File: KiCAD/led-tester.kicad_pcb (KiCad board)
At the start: 2 copper layers, 21 parts, among them IC1 ATMEGA328P-A, P1 CONN_02X07, P2 CONN_01X06, P3 CONN_02X03, U1 MCP1702-5002E

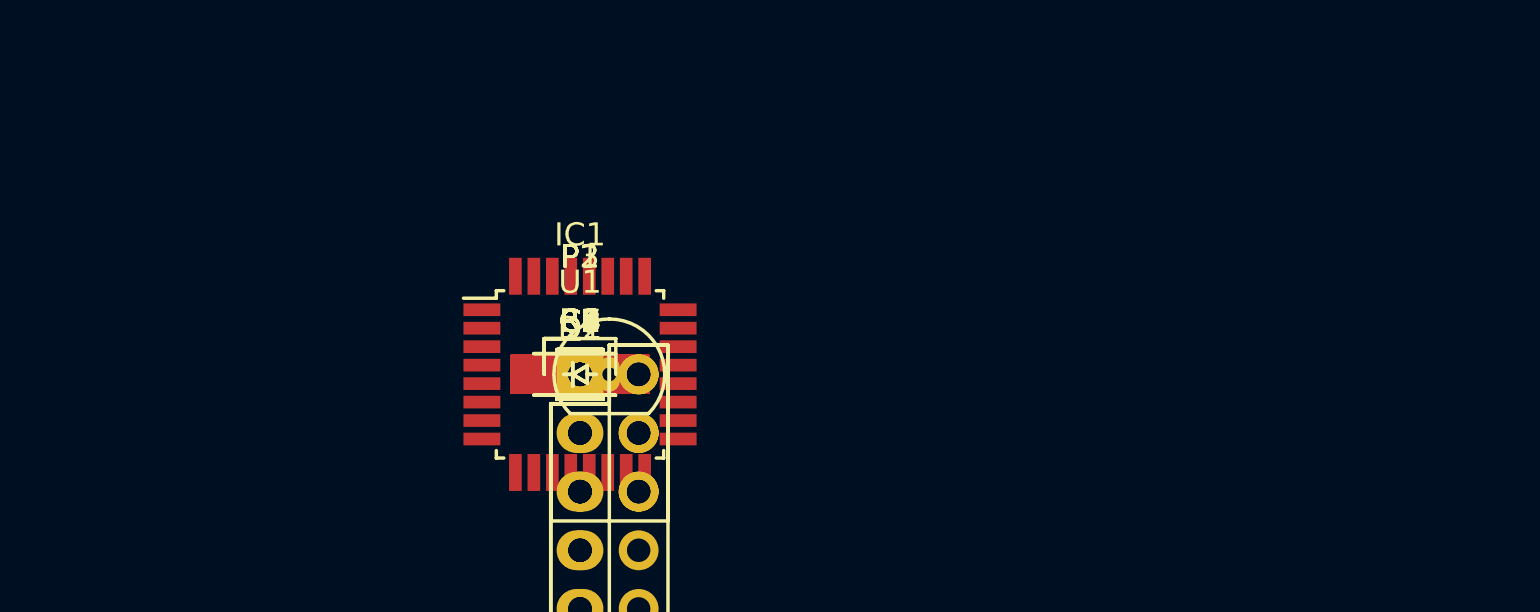
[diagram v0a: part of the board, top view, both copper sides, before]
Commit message: added footprint for led test pads and added pin numbers
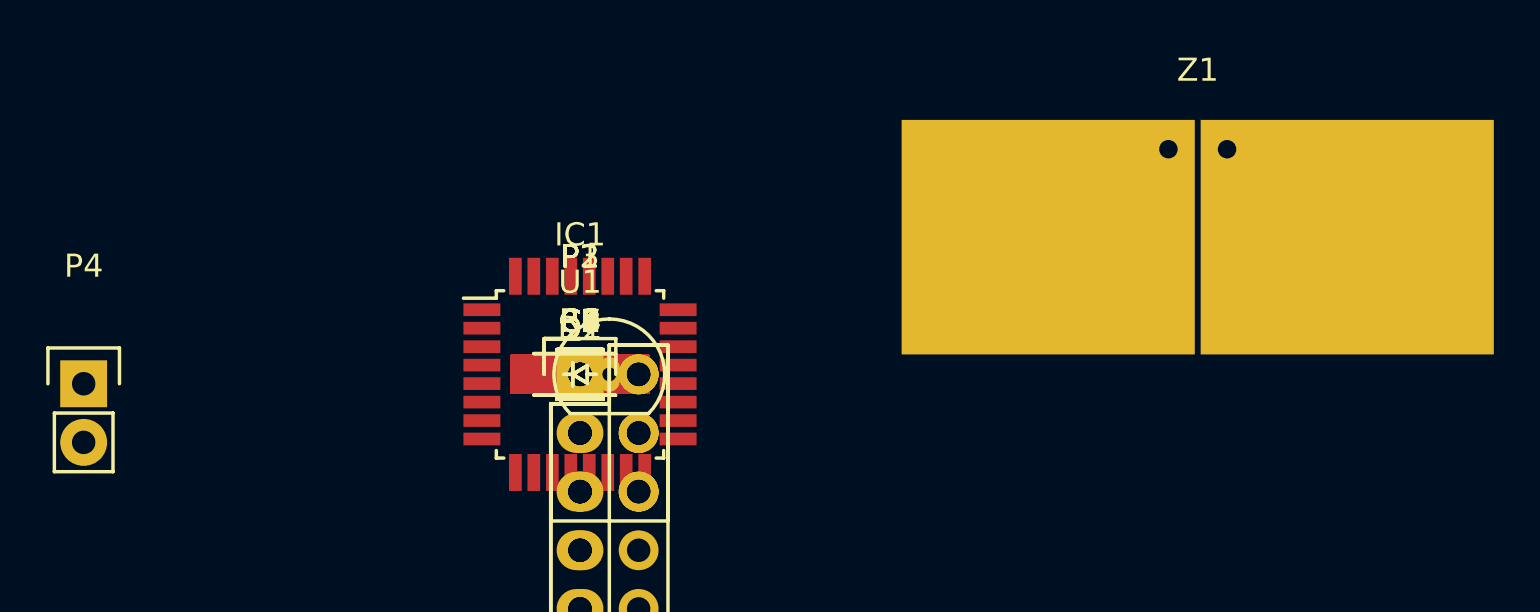
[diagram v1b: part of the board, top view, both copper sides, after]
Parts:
- added P4: CONN_01X02, Pin_Headers:Pin_Header_Straight_1x02, F.Cu at (127.0, 105.4)
- added Z1: testPad, led-tester:LED-LargePads, F.Cu at (175.3, 95.2)
- C1: value 1 uF -> 0.1 uF
- C2: value 0.1 uF -> 1 uF
- C3: value 0.1 uF -> 0.1uF
- C4: value 10 nF -> 0.1uF
- IC1: value ATMEGA328P-A -> ATTINY1634R-SU
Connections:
- C2 pad 1: Net-(C2-Pad1) -> +5V
- C3 pad 1: +5V -> +9V
- C4 pad 1: Net-(C4-Pad1) -> LEDlow
- C5 pad 1: +9V -> LEDhigh
- IC1 pad 1: /a12 -> Net-(IC1-Pad1)
- IC1 pad 10: Net-(IC1-Pad10) -> GND
- IC1 pad 11: Net-(IC1-Pad11) -> +5V
- IC1 pad 13: Net-(IC1-Pad13) -> /a6
- IC1 pad 15: Net-(IC1-Pad15) -> /a5
- IC1 pad 17: Net-(IC1-Pad17) -> /a4
- IC1 pad 18: Net-(C2-Pad1) -> Net-(IC1-Pad18)
- IC1 pad 2: /a13 -> Net-(D1-Pad2)
- IC1 pad 20: Net-(C4-Pad1) -> Net-(IC1-Pad20)
- IC1 pad 21: GND -> (no net)
- IC1 pad 22: Net-(IC1-Pad22) -> (no net)
- IC1 pad 23: /a4 -> (no net)
- IC1 pad 24: /a5 -> (no net)
- IC1 pad 25: /a6 -> (no net)
- IC1 pad 26: LEDlow -> (no net)
- IC1 pad 27: LEDhigh -> (no net)
- IC1 pad 28: Net-(IC1-Pad28) -> (no net)
- IC1 pad 29: Net-(IC1-Pad29) -> (no net)
- IC1 pad 3: GND -> /a14
- IC1 pad 30: Net-(D1-Pad2) -> (no net)
- IC1 pad 31: Net-(IC1-Pad31) -> (no net)
- IC1 pad 32: /a11 -> (no net)
- IC1 pad 4: +5V -> /a13
- IC1 pad 5: GND -> /a12
- IC1 pad 6: +5V -> /a11
- IC1 pad 8: Net-(IC1-Pad8) -> LEDhigh
- IC1 pad 9: /a14 -> LEDlow
- P2 pad 5: Net-(IC1-Pad31) -> Net-(IC1-Pad1)
- P3 pad 1: Net-(IC1-Pad16) -> Net-(IC1-Pad19)
- P3 pad 3: Net-(IC1-Pad17) -> Net-(IC1-Pad16)
- P3 pad 4: Net-(IC1-Pad15) -> Net-(IC1-Pad20)
- P3 pad 5: Net-(IC1-Pad29) -> Net-(IC1-Pad14)
- R4 pad 2: Net-(IC1-Pad29) -> Net-(IC1-Pad14)

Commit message: changed board setting to be compatible with OSHPark
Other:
- net class Default: clearance 0.2 -> 0.1524; trace_width 0.25 -> 0.1524; via_dia 0.6 -> 0.6858; via_drill 0.4 -> 0.3302
- rule trace_clearance: 0.2 -> 0.1524
- rule trace_min: 0.2 -> 0.1524
- rule via_min_drill: 0.3 -> 0.3302
- rule via_min_size: 0.4 -> 0.6858
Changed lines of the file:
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@@
     (links 50)
     (no_connects 30)
-    (area 0 0 0 0)
+    (area 121.891667 89.97 183.08 122.228601)
     (thickness 1.6)
     (drawings 0)
@@
     (0 F.Cu signal)
     (31 B.Cu signal)
-    (32 B.Adhes user)
-    (33 F.Adhes user)
     (34 B.Paste user)
     (35 F.Paste user)
@@
     (38 B.Mask user)
     (39 F.Mask user)
-    (40 Dwgs.User user)
-    (41 Cmts.User user)
-    (42 Eco1.User user)
-    (43 Eco2.User user)
     (44 Edge.Cuts user)
-    (45 Margin user)
-    (46 B.CrtYd user)
-    (47 F.CrtYd user)
-    (48 B.Fab user)
-    (49 F.Fab user)
   )
   (setup
-    (last_trace_width 0.25)
-    (trace_clearance 0.2)
+    (last_trace_width 0.1524)
+    (trace_clearance 0.1524)
     (zone_clearance 0.508)
     (zone_45_only no)
-    (trace_min 0.2)
+    (trace_min 0.1524)
     (segment_width 0.2)
     (edge_width 0.15)
-    (via_size 0.6)
-    (via_drill 0.4)
-    (via_min_size 0.4)
-    (via_min_drill 0.3)
-    (uvia_size 0.3)
+    (via_size 0.6858)
+    (via_drill 0.3302)
+    (via_min_size 0.6858)
+    (via_min_drill 0.3302)
+    (uvia_size 0.762)
     (uvia_drill 0.1)
     (uvias_allowed no)
-    (uvia_min_size 0.2)
-    (uvia_min_drill 0.1)
+    (uvia_min_size 0)
+    (uvia_min_drill 0)
     (pcb_text_width 0.3)
     (pcb_text_size 1.5 1.5)
@@
   (net 35 "Net-(P4-Pad1)")
   (net_class Default "This is the default net class."
-    (clearance 0.2)
-    (trace_width 0.25)
-    (via_dia 0.6)
-    (via_drill 0.4)
-    (uvia_dia 0.3)
+    (clearance 0.1524)
+    (trace_width 0.1524)
+    (via_dia 0.6858)
+    (via_drill 0.3302)
+    (uvia_dia 0.762)
     (uvia_drill 0.1)
     (add_net +5V)

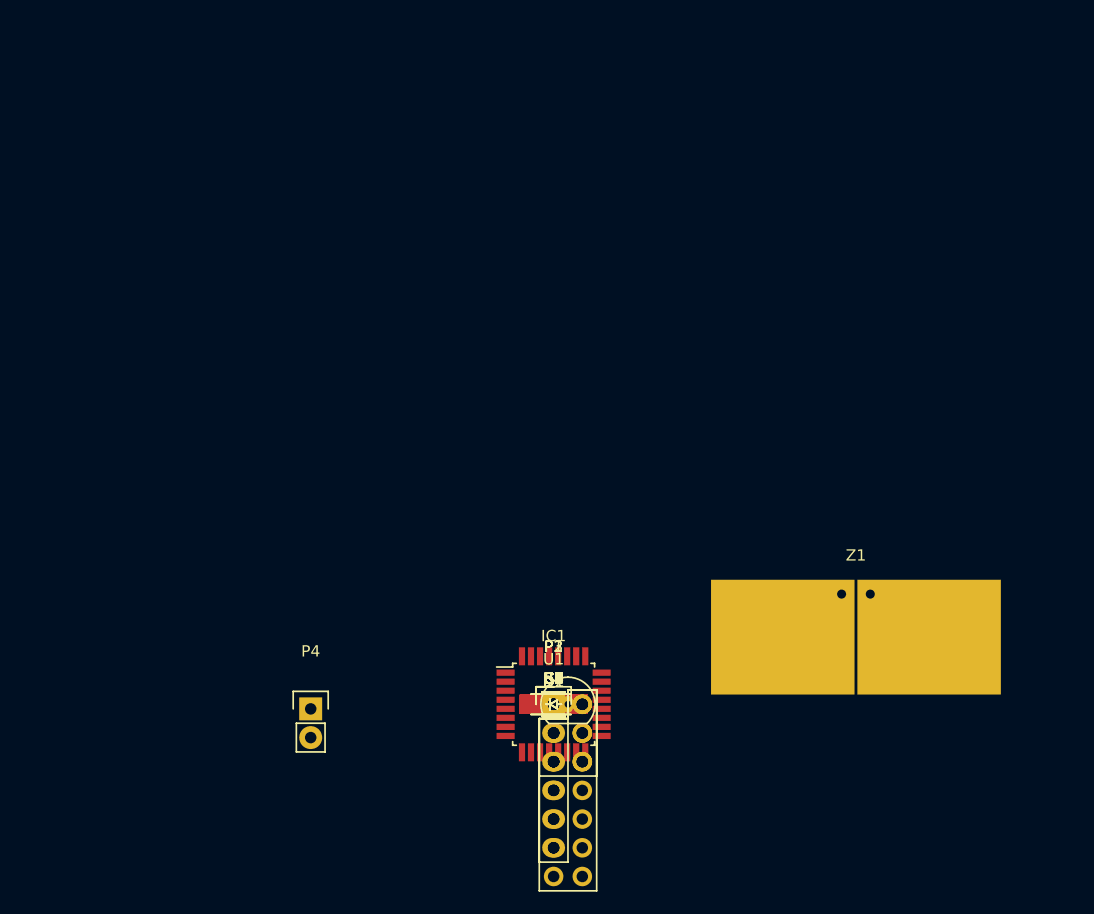
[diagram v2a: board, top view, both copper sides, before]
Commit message: updated project to include new footprints
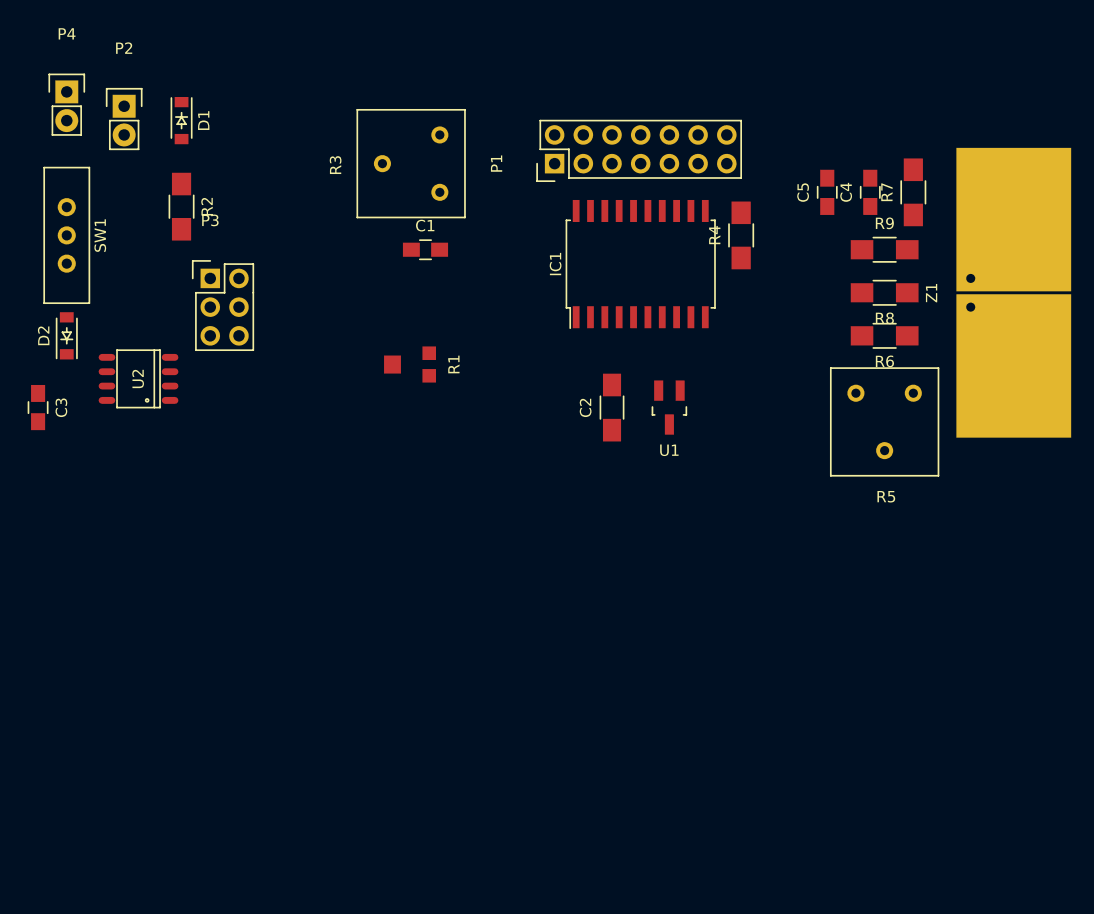
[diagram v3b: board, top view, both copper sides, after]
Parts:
- removed C6, C7: 0.1uF, Capacitors_SMD:C_1206_HandSoldering
- removed C8: 0.1 uF, Capacitors_SMD:C_1206_HandSoldering
- added R1: 10k, led-tester:Panasonic_pot, F.Cu at (135.9, 74.9)
- added R3: 10k, led-tester:bourns_3386_potentiometer, F.Cu at (135.9, 57.1)
- added R5: 500R, led-tester:bourns_3386_potentiometer, F.Cu at (177.8, 80.0)
- added SW1: SWITCH_SPDT, led-tester:SPDT-switch, F.Cu at (105.4, 63.5)
- added U2: LM317LD13TR, Power_Integrations:SO-8, F.Cu at (111.8, 76.2)
- C1, C3, C4, C5: footprint Capacitors_SMD:C_1206_HandSoldering -> Capacitors_SMD:C_0805_HandSoldering
- IC1: footprint Housings_QFP:TQFP-32_7x7mm_Pitch0.8mm -> led-tester:SOIC-20_7.5x12.8mm_Pitch1.27mm
- P2: value CONN_01X06 -> CONN_01X02; footprint Pin_Headers:Pin_Header_Straight_1x06 -> Pin_Headers:Pin_Header_Straight_1x02
- U1: value MCP1702-5002E -> MCP1702T-5002E; footprint TO_SOT_Packages_THT:TO-92_Inline_Narrow_Oval -> TO_SOT_Packages_SMD:SOT-23_Handsoldering
- moved P2 65.2 mm to (110.5, 52.1)
- moved D1 61.3 mm to (115.6, 53.3), turned to 270 degrees
- moved P4 58.7 mm to (105.4, 50.8)
- moved R7 55.4 mm to (180.3, 59.7), turned to 90 degrees
- moved R2 55.0 mm to (115.6, 61.0), turned to 270 degrees
- moved D2 54.0 mm to (105.4, 72.4), turned to 90 degrees
- moved C4 53.3 mm to (176.5, 59.7), turned to 90 degrees
- moved C3 52.6 mm to (102.9, 78.7), turned to 270 degrees
- moved C5 51.4 mm to (172.7, 59.7), turned to 90 degrees
- moved R9 49.8 mm to (177.8, 64.8)
- moved P3 48.4 mm to (118.1, 67.3)
- moved P1 47.9 mm to (148.6, 57.1), turned to 90 degrees
- moved R8 46.7 mm to (177.8, 68.6), turned to 180 degrees
- moved R4 44.7 mm to (165.1, 63.5), turned to 90 degrees
- moved R6 43.8 mm to (177.8, 72.4), turned to 180 degrees
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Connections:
- P2 pad 2: Net-(P2-Pad2) -> Net-(D1-Pad1)

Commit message: converted to hierarchical sheets and added MPN field to components
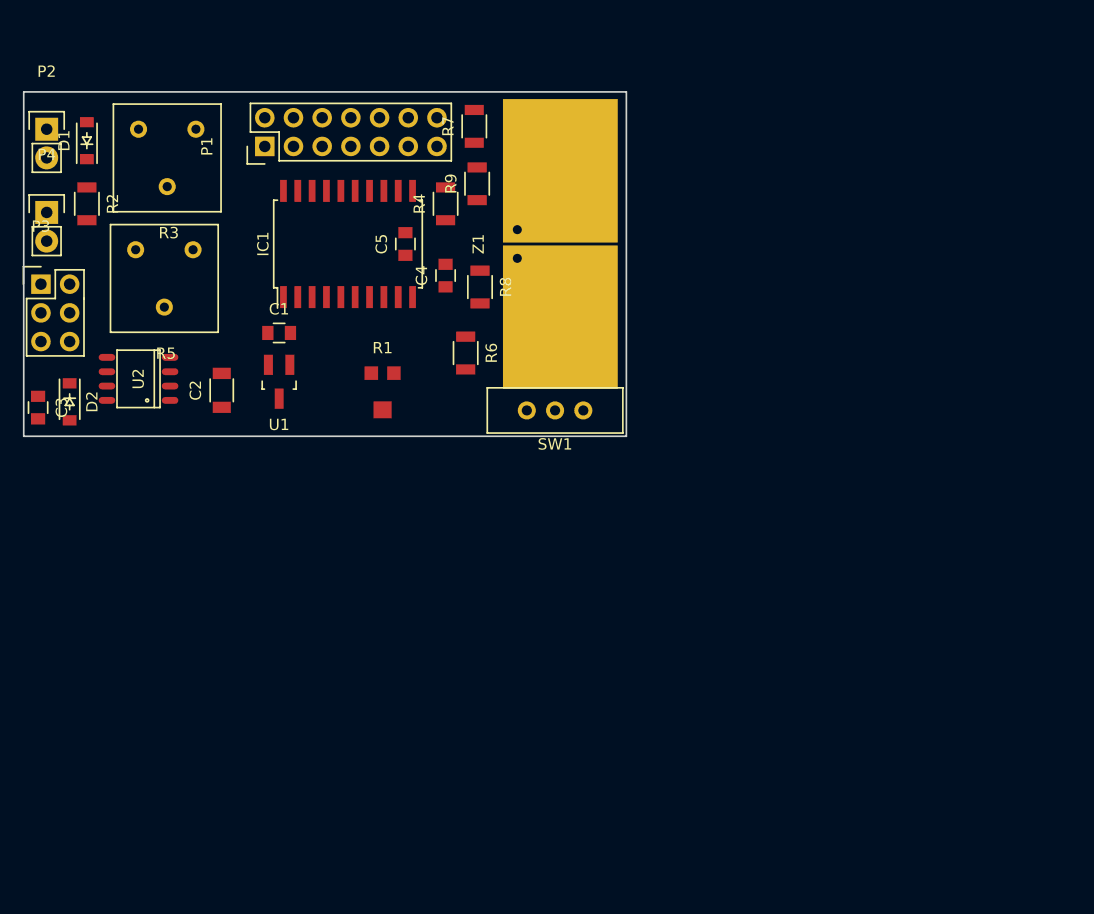
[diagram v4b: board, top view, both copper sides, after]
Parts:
- C1, C3, C4, C5: footprint Capacitors_SMD:C_0805_HandSoldering -> Capacitors_SMD:C_0805
- C2: value 1 uF -> 2.2 uF; footprint Capacitors_SMD:C_1206_HandSoldering -> Capacitors_SMD:C_1206
- D1, D2: value RB161M-20TR -> Schottky
- IC1: value ATTINY1634R-SU -> ATTINY1634
- R2, R4, R6, R7, R8, R9: footprint Resistors_SMD:R_1206_HandSoldering -> Resistors_SMD:R_1206
- U1: value MCP1702T-5002E -> MCP1702
- U2: value LM317LD13TR -> LM317L
- moved R5 65.0 mm to (114.0, 67.3)
- moved SW1 45.9 mm to (148.6, 79.0), turned to 0 degrees
- moved Z1 40.4 mm to (145.3, 64.3)
- moved R7 39.3 mm to (141.5, 53.8)
- moved C4 38.3 mm to (138.9, 67.1)
- moved C5 37.6 mm to (135.4, 64.3)
- moved R6 37.1 mm to (140.7, 73.9), turned to 270 degrees
- moved R9 36.5 mm to (141.7, 58.9), turned to 90 degrees
- moved R8 35.8 mm to (142.0, 68.1), turned to 270 degrees
- moved U1 34.6 mm to (124.2, 76.5)
- moved C2 34.6 mm to (119.1, 77.2)
- moved R4 26.3 mm to (138.9, 60.7)
- moved IC1 26.0 mm to (130.3, 64.3)
- moved P1 25.7 mm to (122.9, 55.6)
- moved R3 21.6 mm to (114.3, 56.6), turned to 0 degrees
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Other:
- board outline added: 53.3 x 30.5 mm

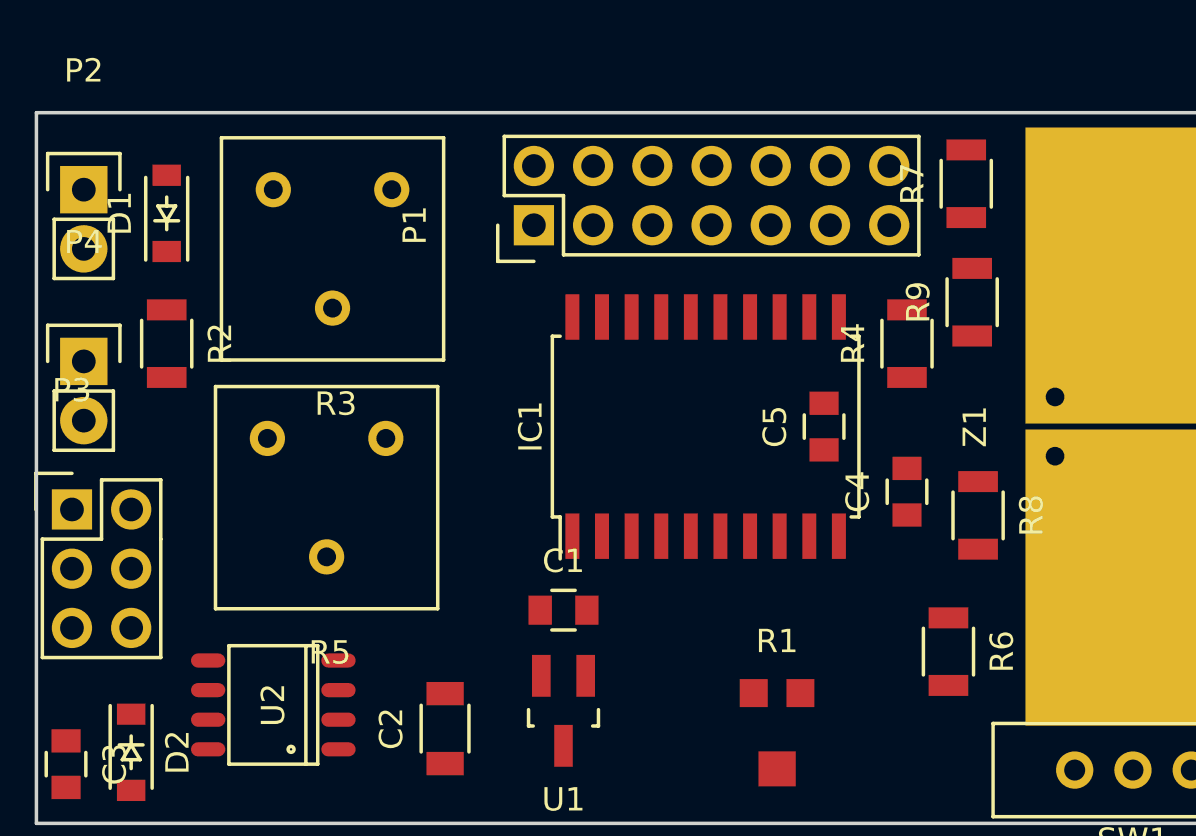
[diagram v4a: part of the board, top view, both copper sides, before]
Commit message: reorganized digitalDisplay sheet and pulled LED pads to top sheet
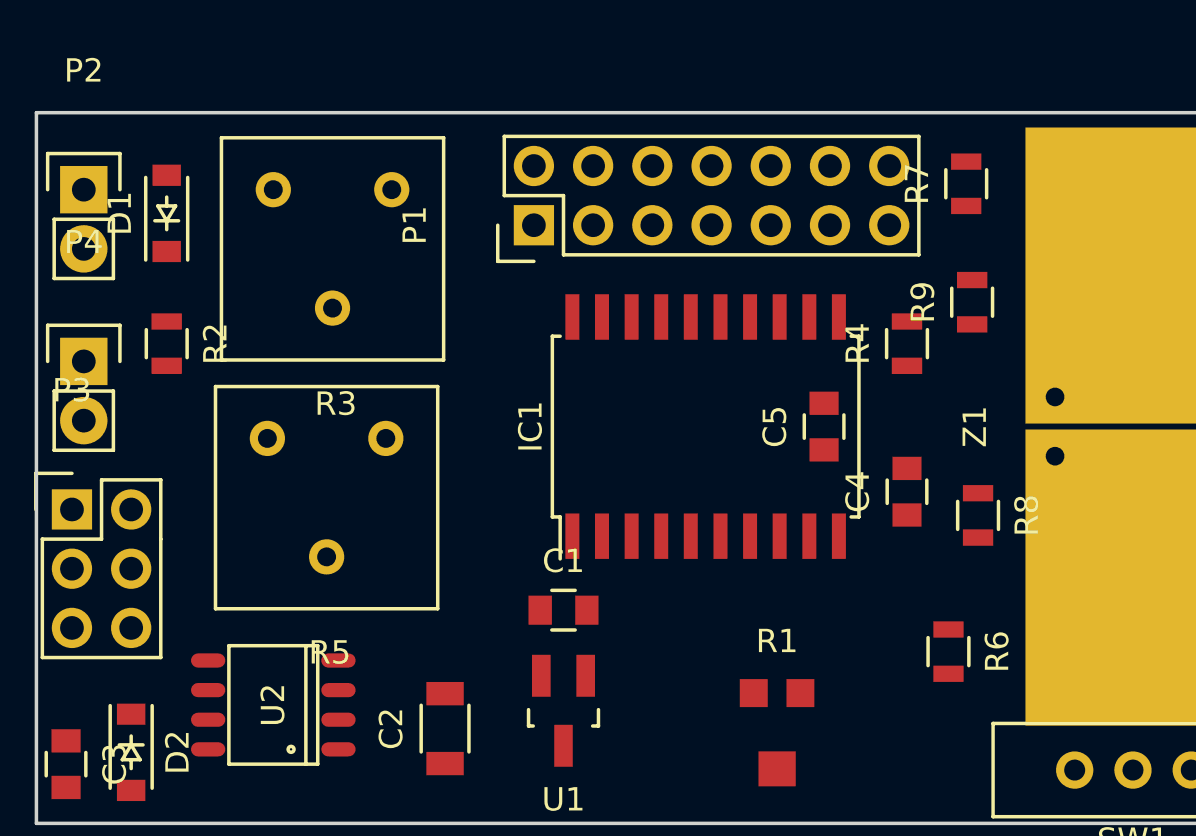
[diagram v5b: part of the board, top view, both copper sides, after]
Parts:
- R2, R4, R6, R7, R8, R9: footprint Resistors_SMD:R_1206 -> Resistors_SMD:R_0805
